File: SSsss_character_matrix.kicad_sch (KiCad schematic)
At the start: 14 parts, among them U15 SN74LVC244A, U16 SM411006N/15, U17 SM411006N/15, U18 SN74LVC244A, U19 SM411006N/15, U20 SM411006N/15, U21 SM411006N/15

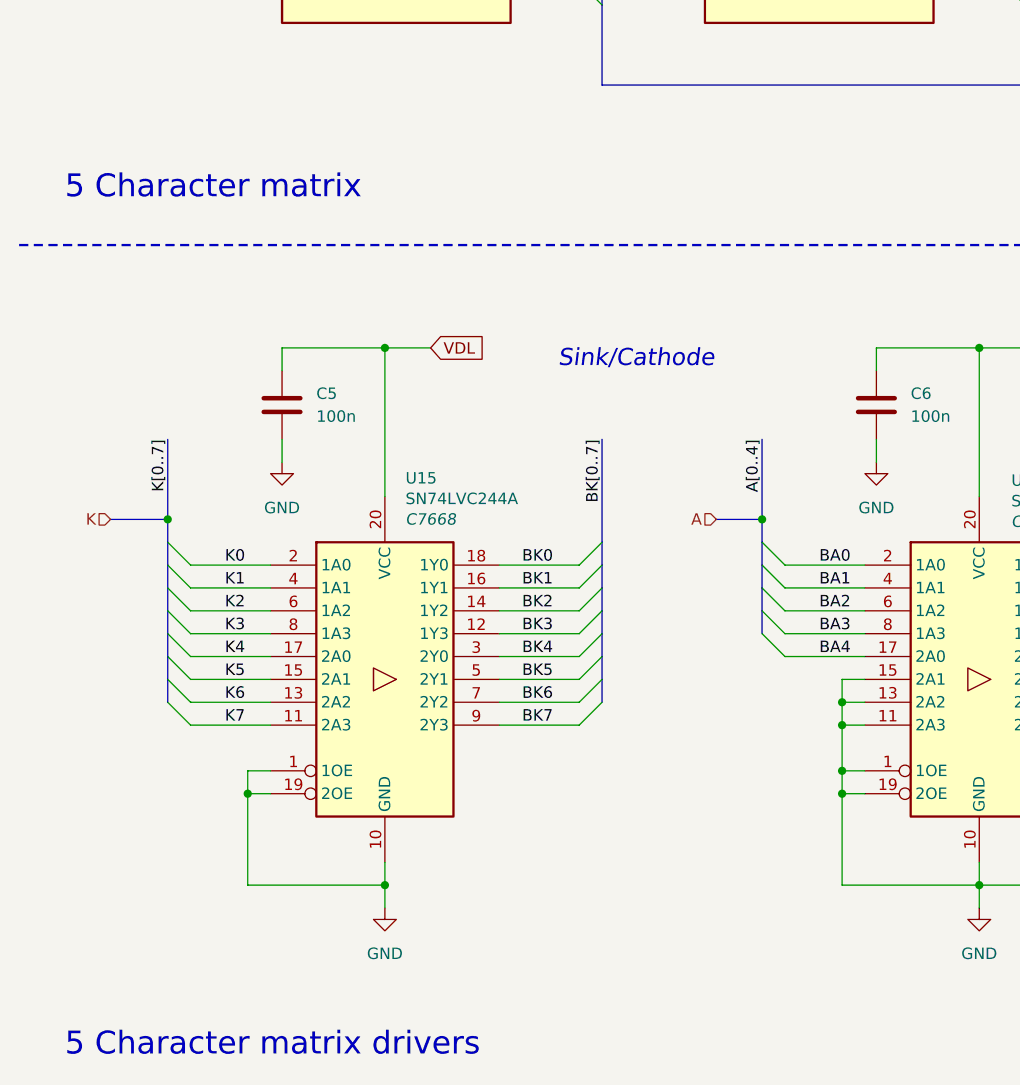
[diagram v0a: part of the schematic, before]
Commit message: addition of bus
- cleaned up the structure of the schematic.
- addition of the colon
- root schematic improvements
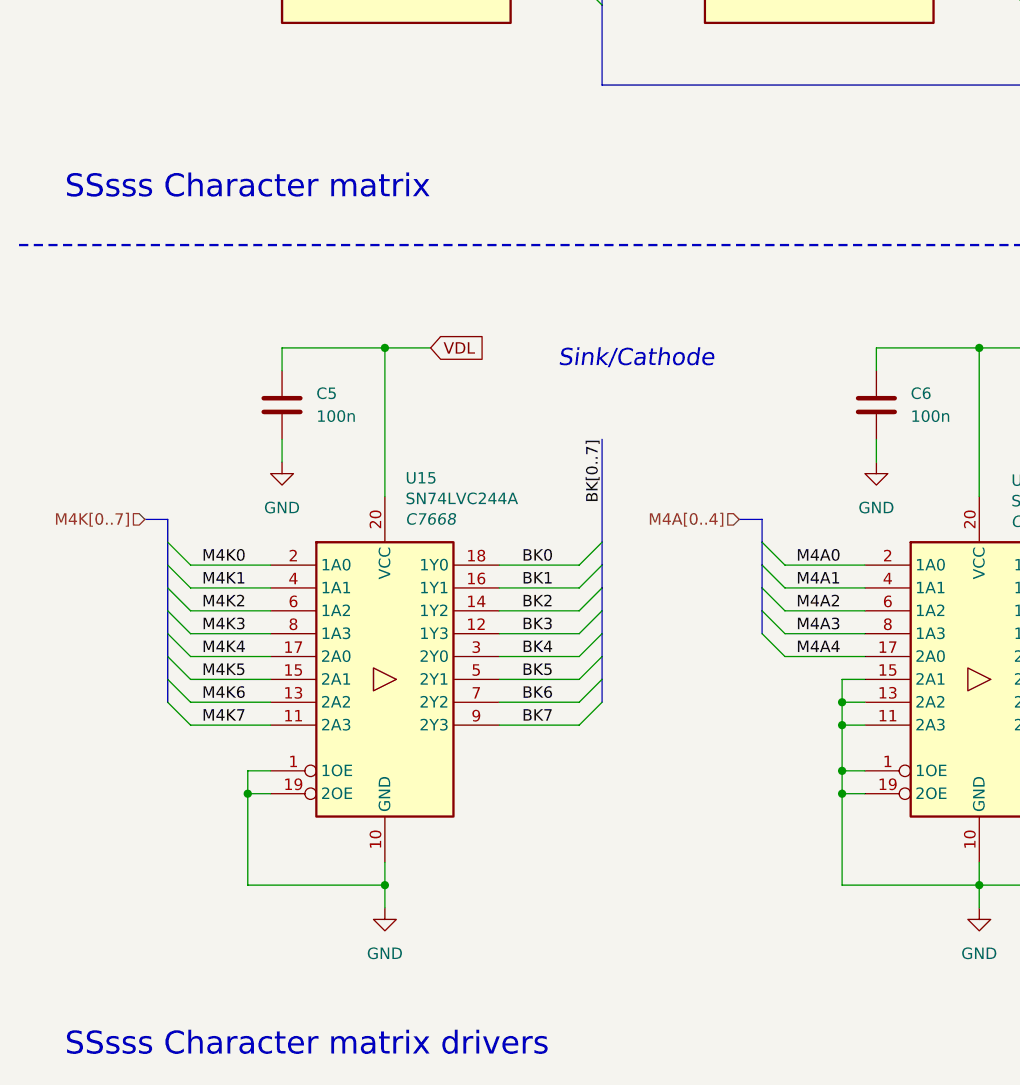
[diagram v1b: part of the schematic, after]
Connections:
- net BA0: no longer U18.2 (1A0)
- net BA1: no longer U18.4 (1A1)
- net BA2: no longer U18.6 (1A2)
- net BA3: no longer U18.8 (1A3)
- net BA4: no longer U18.17 (2A0)
- net K0 renamed M4K0
- net K1 renamed M4K1
- net K2 renamed M4K2
- net K3 renamed M4K3
- net K4 renamed M4K4
- net K5 renamed M4K5
- net K6 renamed M4K6
- net K7 renamed M4K7
- new net M4A0: U18.2 (1A0)
- new net M4A1: U18.4 (1A1)
- new net M4A2: U18.6 (1A2)
- new net M4A3: U18.8 (1A3)
- new net M4A4: U18.17 (2A0)
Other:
- note added: "SSsss Character matrix"
- note added: "SSsss Character matrix drivers"
- note removed: "5 Character matrix"
- note removed: "5 Character matrix drivers"
- title: 5 Character Matrix & Drivers  -> SSsss Character Matrix & Drivers 

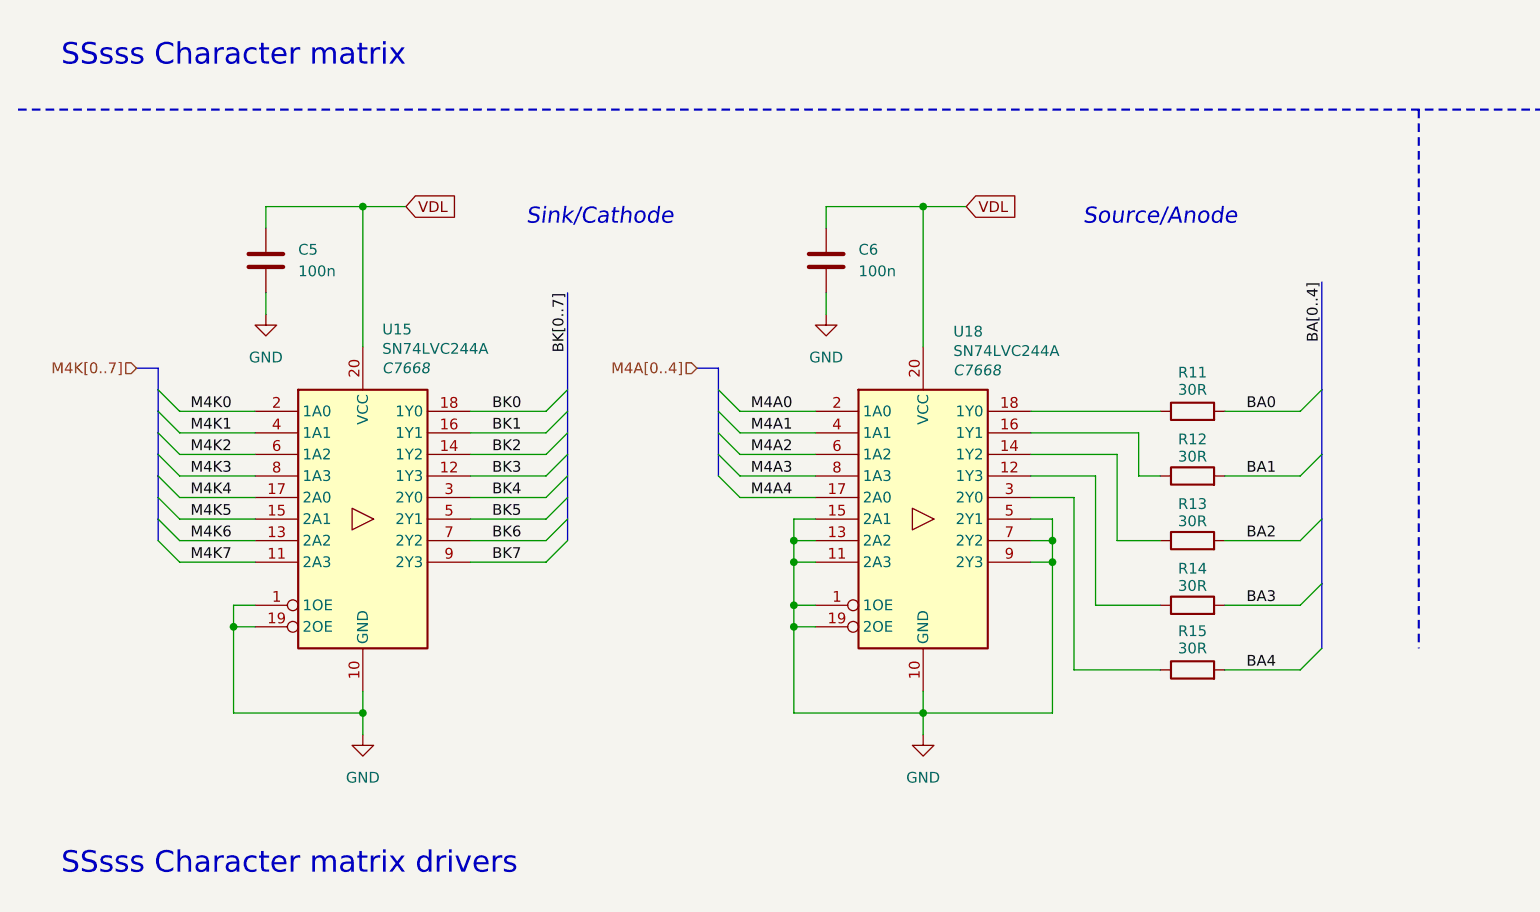
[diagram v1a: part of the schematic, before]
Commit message: current limiting resistor changes
- added colon led model, but might replace it in the future.
- reduction in current limiting resistance.
- removed the solder jumps in the individual circuit schematics.
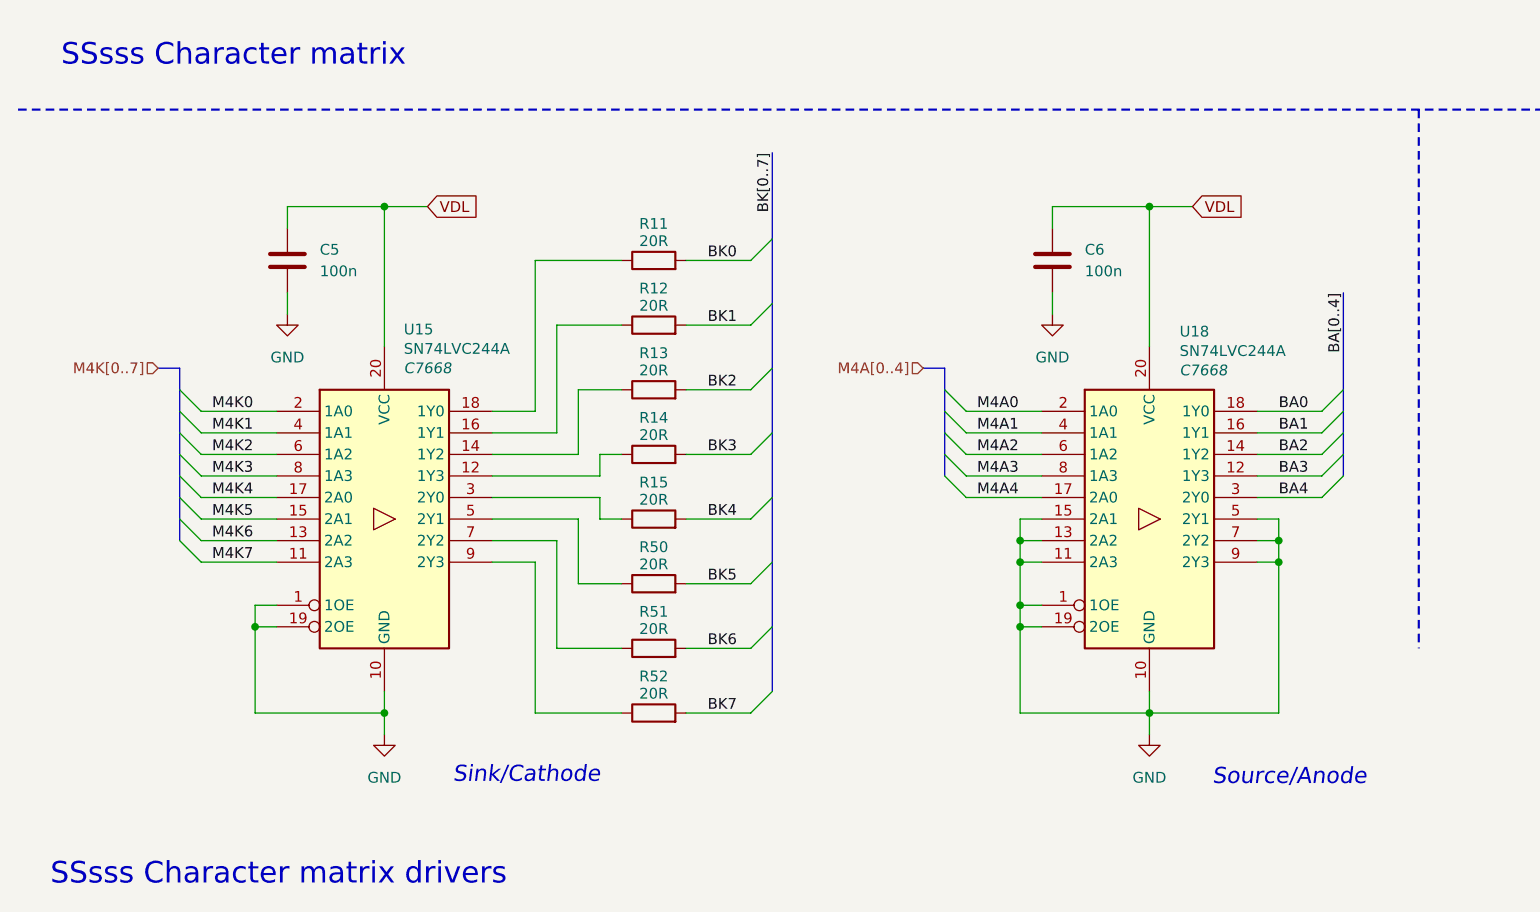
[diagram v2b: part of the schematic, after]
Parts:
- added R50, R51, R52: 20R, symbol Device:R
- R11, R12, R13, R14, R15: value 30R -> 20R
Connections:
- net BA0: now also U18.18 (1Y0); no longer R11.2
- net BA1: now also U18.16 (1Y1); no longer R12.2
- net BA2: now also U18.14 (1Y2); no longer R13.2
- net BA3: now also U18.12 (1Y3); no longer R14.2
- net BA4: now also U18.3 (2Y0); no longer R15.2
- net BK0: now also R11.2; no longer U15.18 (1Y0)
- net BK1: now also R12.2; no longer U15.16 (1Y1)
- net BK2: now also R13.2; no longer U15.14 (1Y2)
- net BK3: now also R14.2; no longer U15.12 (1Y3)
- net BK4: now also R15.2; no longer U15.3 (2Y0)
- net BK5: now also R50.2; no longer U15.5 (2Y1)
- net BK6: now also R51.2; no longer U15.7 (2Y2)
- net BK7: now also R52.2; no longer U15.9 (2Y3)
- net at R11.1: now also U15.18 (1Y0); no longer U18.18 (1Y0)
- net at R13.1: now also U15.14 (1Y2); no longer U18.14 (1Y2)
- net at R14.1: now also U15.12 (1Y3); no longer U18.12 (1Y3)
- net at R12.1: now also U15.16 (1Y1); no longer U18.16 (1Y1)
- net at R15.1: now also U15.3 (2Y0); no longer U18.3 (2Y0)
- new net: R50.1, U15.5 (2Y1)
- new net: R51.1, U15.7 (2Y2)
- new net: R52.1, U15.9 (2Y3)

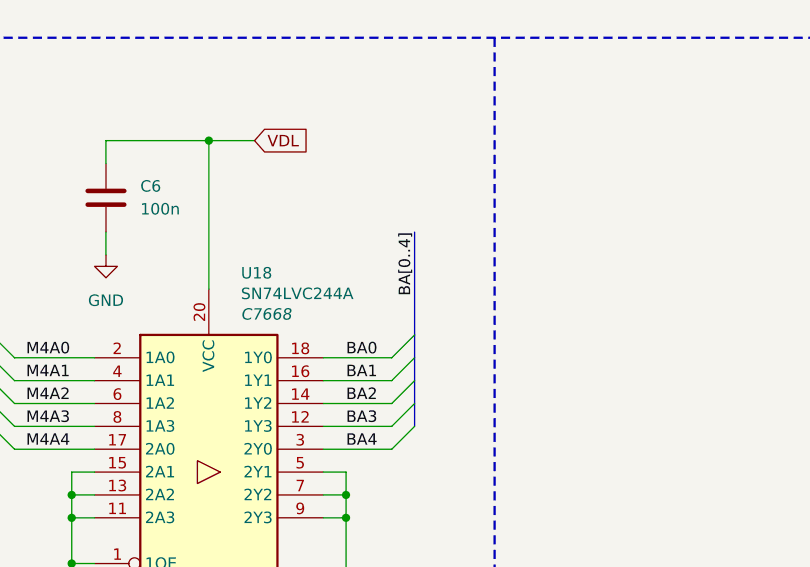
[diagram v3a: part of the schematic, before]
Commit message: Buzzer driver added - replacement of photoresistor to a variable resistor - added button - general formatting
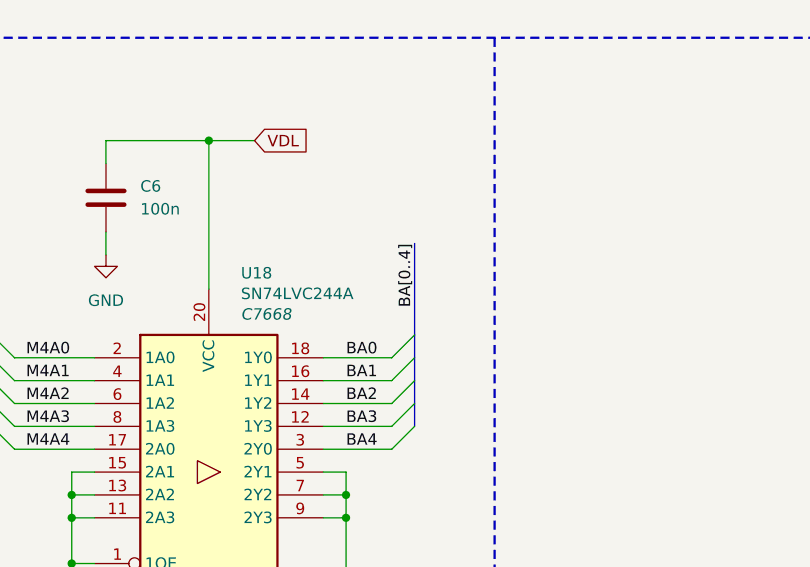
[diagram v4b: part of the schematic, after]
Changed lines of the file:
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@@
 	(bus
 		(pts
-			(xy 168.91 123.19) (xy 168.91 134.62)
+			(xy 168.91 124.46) (xy 168.91 134.62)
 		)
 		(stroke
@@
 	)
 	(label "BA[0..4]"
-		(at 168.91 123.19 270)
-		(effects
-			(font
+		(at 168.91 124.46 270)
+		(effects
+			(font

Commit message: ESD, LEDs, footprints
- assignment of footprints
- ESD protection
- User buttons
- addition of test points
- BOM consolidation of  resistors
- general reordering of the schematic
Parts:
- C5, C6: footprint (none) -> Capacitor_SMD:C_0603_1608Metric
- R11, R12, R13, R14, R15, R50, R51, R52: footprint (none) -> Resistor_SMD:R_0603_1608Metric
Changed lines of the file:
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@@
 	(title_block
 		(title "SSsss Character Matrix & Drivers ")
-		(date "2025-10-31")
+		(date "2025-11-04")
 		(rev "v0.0")
 		(company "Rajath Katker")
@@
 			)
 		)
-		(property "Footprint" ""
+		(property "Footprint" "Resistor_SMD:R_0603_1608Metric"
 			(at 87.63 159.258 90)
 			(effects
@@
 			)
 		)
-		(property "Footprint" ""
+		(property "Footprint" "Resistor_SMD:R_0603_1608Metric"
 			(at 87.63 128.778 90)
 			(effects
@@
 			)
 		)
-		(property "Footprint" ""
+		(property "Footprint" "Capacitor_SMD:C_0603_1608Metric"
 			(at 45.4152 123.19 0)
 			(effects
@@
 			)
 		)
-		(property "Footprint" ""
+		(property "Footprint" "Resistor_SMD:R_0603_1608Metric"
 			(at 87.63 166.878 90)
 			(effects
@@
 			)
 		)
-		(property "Footprint" ""
+		(property "Footprint" "Resistor_SMD:R_0603_1608Metric"
 			(at 87.63 121.158 90)
 			(effects
@@
 			)
 		)
-		(property "Footprint" ""
+		(property "Footprint" "Resistor_SMD:R_0603_1608Metric"
 			(at 87.63 151.638 90)
 			(effects
@@
 			)
 		)
-		(property "Footprint" ""
+		(property "Footprint" "Resistor_SMD:R_0603_1608Metric"
 			(at 87.63 174.498 90)
 			(effects
@@
 			)
 		)
-		(property "Footprint" ""
+		(property "Footprint" "Resistor_SMD:R_0603_1608Metric"
 			(at 87.63 136.398 90)
 			(effects
@@
 			)
 		)
-		(property "Footprint" ""
+		(property "Footprint" "Capacitor_SMD:C_0603_1608Metric"
 			(at 135.5852 123.19 0)
 			(effects
@@
 			)
 		)
-		(property "Footprint" ""
+		(property "Footprint" "Resistor_SMD:R_0603_1608Metric"
 			(at 87.63 144.018 90)
 			(effects
